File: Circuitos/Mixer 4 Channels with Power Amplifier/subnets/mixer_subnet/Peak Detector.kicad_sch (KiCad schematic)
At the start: 13 parts

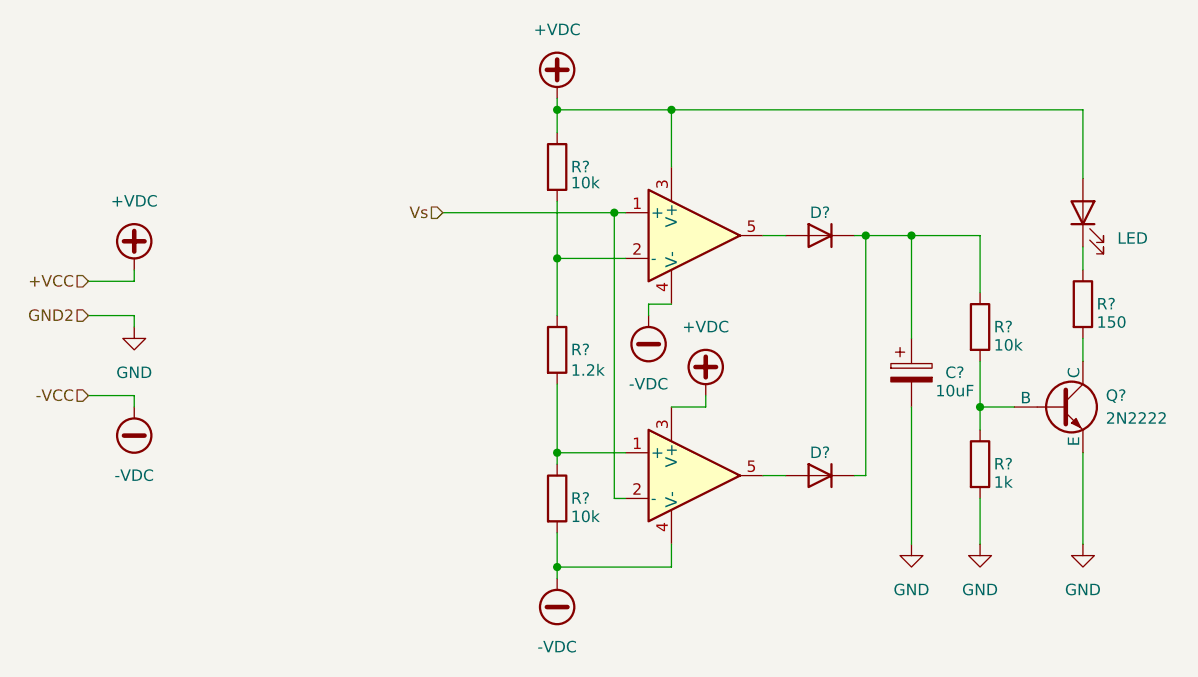
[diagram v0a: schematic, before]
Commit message: Correcciones y modificaciones en fuente, amp auriculares y simul completa
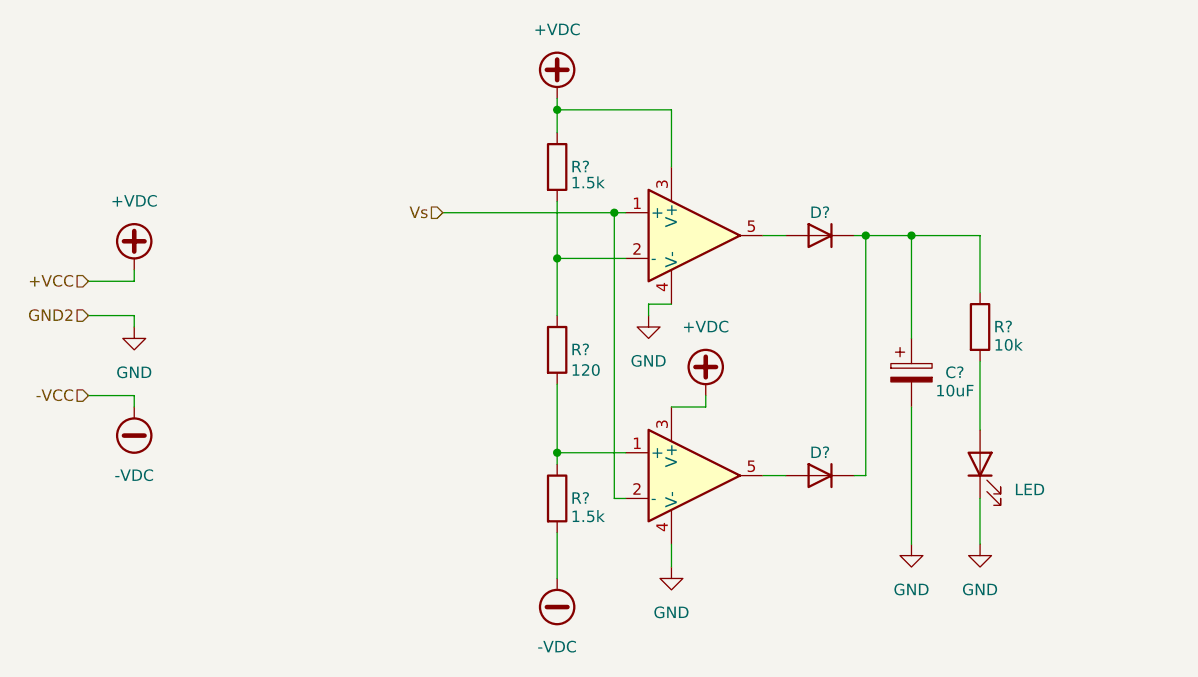
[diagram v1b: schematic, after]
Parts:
- removed Q?: 2N2222, symbol Simulation_SPICE:NPN
- removed R?: 150, symbol Device:R
- removed R?: 1k, symbol Device:R
- R?: value 1.2k -> 120
- R? (x2): value 10k -> 1.5k
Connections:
- net +VDC: no longer D?.2 (A)
- net -VDC: no longer U?.4 (V-), U?.4 (V-)
- net GND: now also D?.1 (K), U?.4 (V-), U?.4 (V-)
- net at R?.2: now also D?.2 (A)

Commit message: Informe finalizado
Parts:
- C?: value 10uF -> 100p
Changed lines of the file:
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@@
 			)
 		)
-		(property "Value" "10uF"
+		(property "Value" "100p"
 			(at 167.386 101.092 0)
 			(effects
